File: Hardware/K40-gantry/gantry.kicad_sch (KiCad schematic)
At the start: 10 parts, among them U101 TCST1030, U102 TCST1030

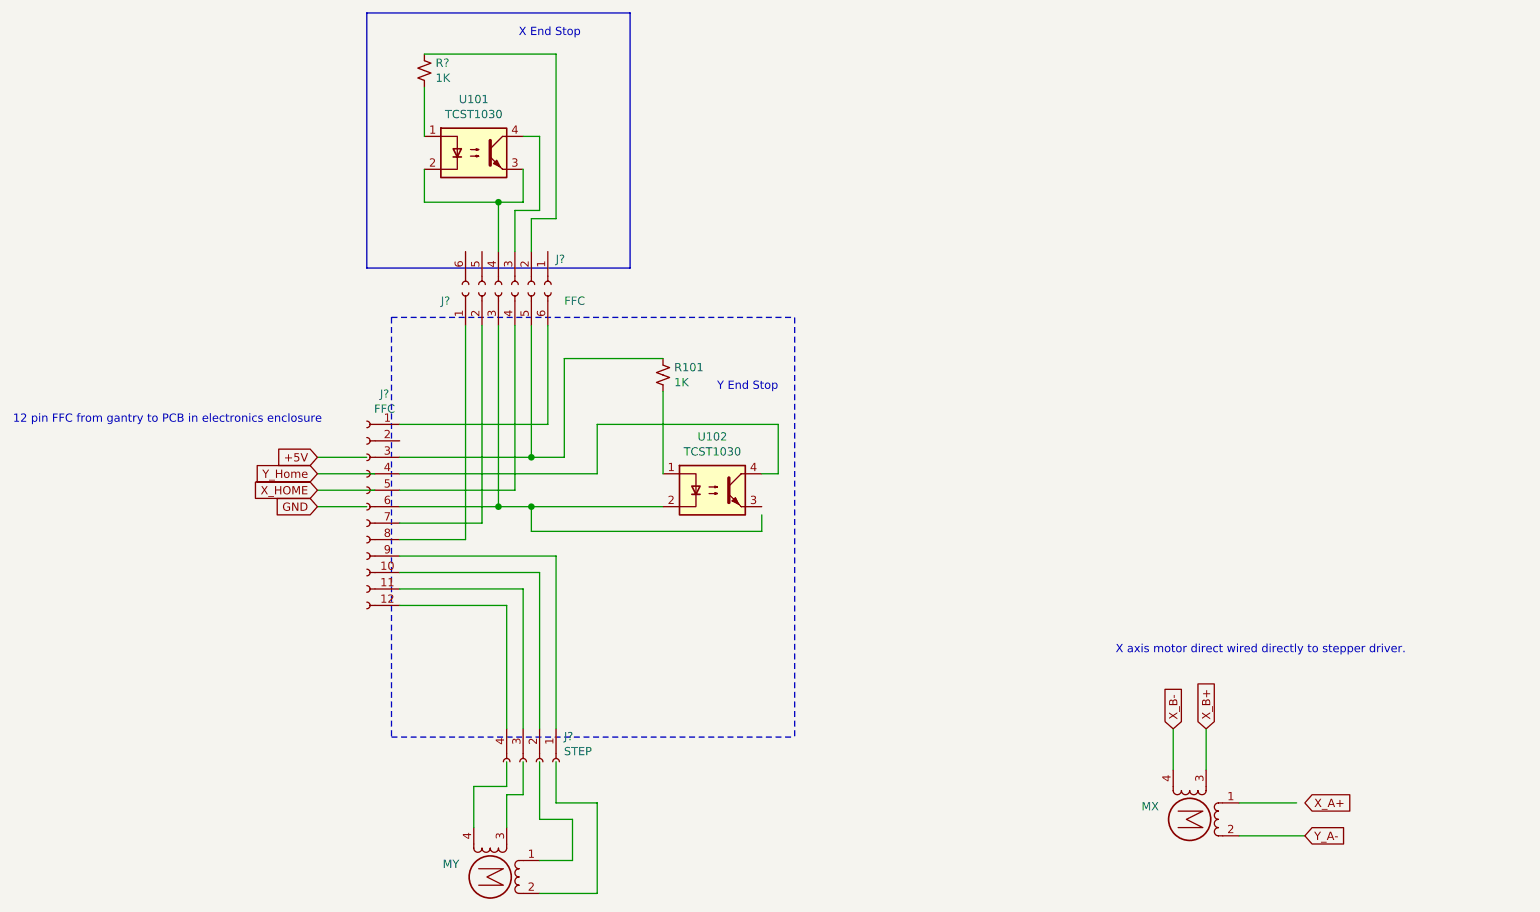
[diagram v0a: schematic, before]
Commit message: Added PDF of schematic
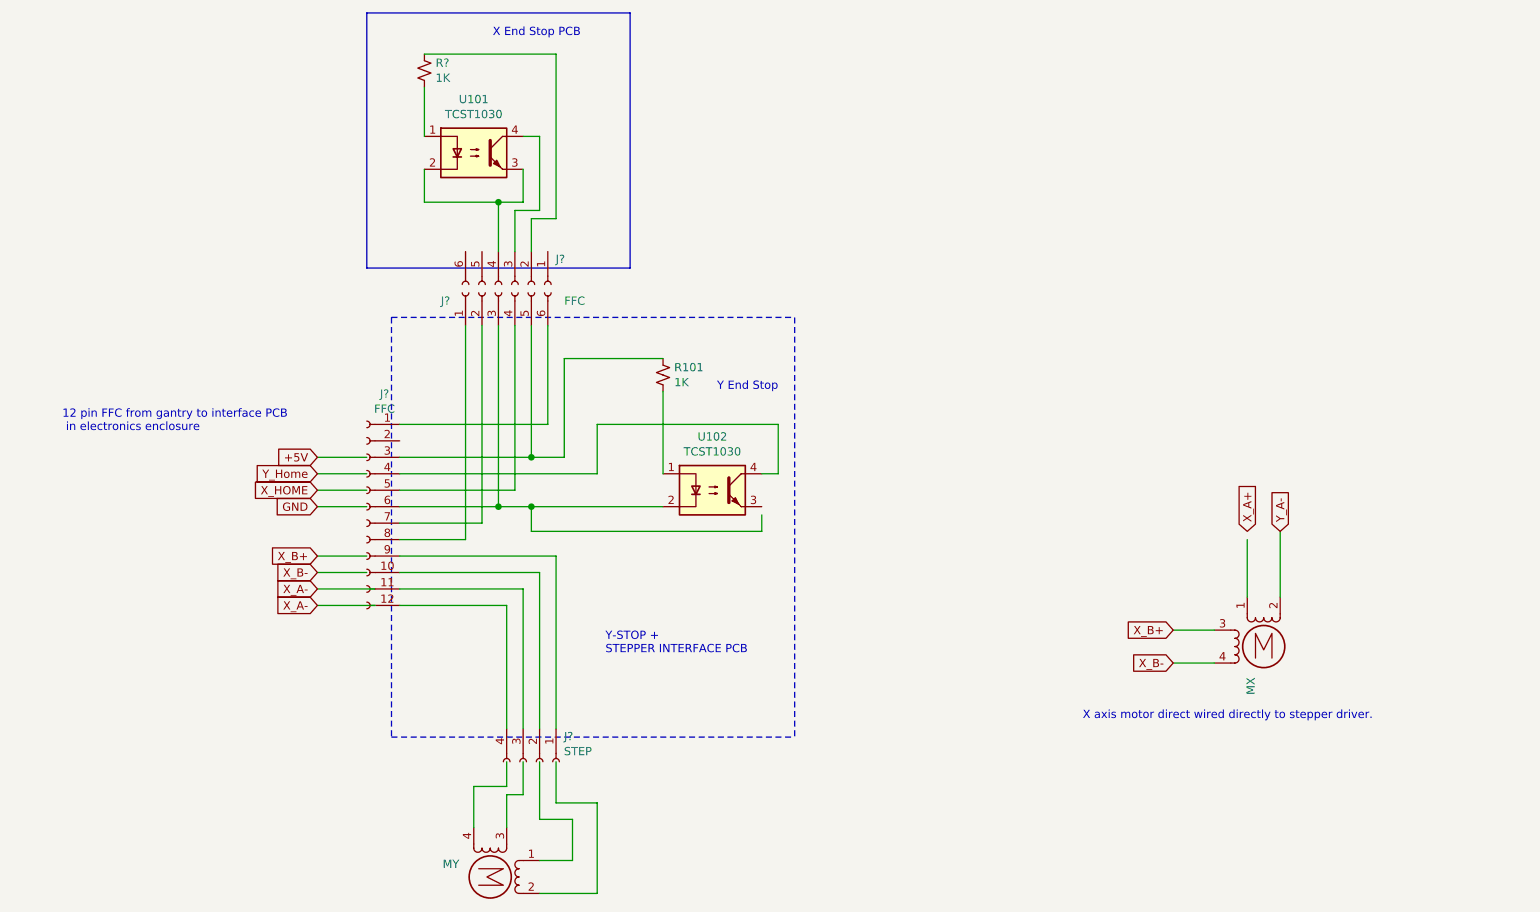
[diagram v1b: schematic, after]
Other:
- note added: "12 pin FFC from gantry to interface PCB in electronics enclosure"
- note added: "X End Stop PCB"
- note added: "Y-STOP + STEPPER INTERFACE PCB"
- note removed: "12 pin FFC from gantry to PCB in electronics enclosure"
- note removed: "X End Stop"
- company: Geoff Steer -> Hobart Makers
- moved on the sheet: MX
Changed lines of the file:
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@@
     (title "K40 Laser Gantry wiring")
     (date "2021-07-31")
-    (company "Geoff Steer")
+    (rev "1")
+    (company "Hobart Makers")
+    (comment 1 "Geoff Steer")
+    (comment 3 "Circuit diagram copied from https://donsthings.blogspot.com")
   )
   (junction (at 101.6 50.8) (diameter 1.016) (color 0 0 0 0))
@@
   (junction (at 106.68 90.17) (diameter 1.016) (color 0 0 0 0))
   (junction (at 106.68 97.79) (diameter 1.016) (color 0 0 0 0))
-  (wire (pts (xy 73.66 92.71) (xy 82.55 92.71))
-    (stroke (width 0) (type solid) (color 0 0 0 0))
-  )
-  (wire (pts (xy 73.66 95.25) (xy 82.55 95.25))
+  (wire (pts (xy 73.66 92.71) (xy 81.28 92.71))
+    (stroke (width 0) (type solid) (color 0 0 0 0))
+  )
+  (wire (pts (xy 73.66 95.25) (xy 81.28 95.25))
     (stroke (width 0) (type solid) (color 0 0 0 0))
   )
@@
     (stroke (width 0) (type solid) (color 0 0 0 0))
   )
+  (wire (pts (xy 73.66 105.41) (xy 81.28 105.41))
+    (stroke (width 0) (type solid) (color 0 0 0 0))
+  )
+  (wire (pts (xy 73.66 107.95) (xy 81.28 107.95))
+    (stroke (width 0) (type solid) (color 0 0 0 0))
+  )
+  (wire (pts (xy 73.66 110.49) (xy 82.55 110.49))
+    (stroke (width 0) (type solid) (color 0 0 0 0))
+  )
+  (wire (pts (xy 73.66 113.03) (xy 82.55 113.03))
+    (stroke (width 0) (type solid) (color 0 0 0 0))
+  )
   (wire (pts (xy 81.28 90.17) (xy 73.66 90.17))
     (stroke (width 0) (type solid) (color 0 0 0 0))
@@
     (stroke (width 0) (type solid) (color 0 0 0 0))
   )
-  (wire (pts (xy 205.74 138.43) (xy 205.74 132.08))
-    (stroke (width 0) (type solid) (color 0 0 0 0))
-  )
-  (wire (pts (xy 210.82 132.08) (xy 210.82 138.43))
-    (stroke (width 0) (type solid) (color 0 0 0 0))
-  )
-  (wire (pts (xy 224.79 143.51) (xy 215.9 143.51))
-    (stroke (width 0) (type solid) (color 0 0 0 0))
-  )
-  (wire (pts (xy 226.06 148.59) (xy 215.9 148.59))
+  (wire (pts (xy 205.74 116.84) (xy 212.09 116.84))
+    (stroke (width 0) (type solid) (color 0 0 0 0))
+  )
+  (wire (pts (xy 212.09 121.92) (xy 205.74 121.92))
+    (stroke (width 0) (type solid) (color 0 0 0 0))
+  )
+  (wire (pts (xy 217.17 102.87) (xy 217.17 111.76))
+    (stroke (width 0) (type solid) (color 0 0 0 0))
+  )
+  (wire (pts (xy 222.25 101.6) (xy 222.25 111.76))
     (stroke (width 0) (type solid) (color 0 0 0 0))
   )
@@
     (stroke (width 0) (type dash) (color 0 0 0 0))
   )
-  (text "12 pin FFC from gantry to PCB in electronics enclosure"
-    (at 26.67 85.09 0)
+  (text "12 pin FFC from gantry to interface PCB\n in electronics enclosure"
+    (at 34.29 86.36 0)
     (effects (font (size 1.27 1.27)) (justify left bottom))
   )
-  (text "X End Stop" (at 114.3 25.4 180)
+  (text "X End Stop PCB" (at 114.3 25.4 180)
     (effects (font (size 1.27 1.27)) (justify right bottom))
+  )
+  (text "Y-STOP + \nSTEPPER INTERFACE PCB" (at 118.11 120.65 0)
+    (effects (font (size 1.27 1.27)) (justify left bottom))
   )
   (text "Y End Stop" (at 144.78 80.01 180)
@@
   )
   (text "X axis motor direct wired directly to stepper driver."
-    (at 196.85 120.65 0)
+    (at 191.77 130.81 0)
     (effects (font (size 1.27 1.27)) (justify left bottom))
   )
@@
     )
   )
-  (global_label "X_B-" (shape input) (at 205.74 132.08 90) (fields_autoplaced)
+  (global_label "X_B+" (shape input) (at 73.66 105.41 180) (fields_autoplaced)
+    (effects (font (size 1.27 1.27)) (justify right))
+    (property "Intersheet References" "${INTERSHEET_REFS}" (id 0) (at -58.42 316.23 0)
+      (effects (font (size 1.27 1.27)) hide)
+    )
+  )
+  (global_label "X_B-" (shape input) (at 73.66 107.95 180) (fields_autoplaced)
+    (effects (font (size 1.27 1.27)) (justify right))
+    (property "Intersheet References" "${INTERSHEET_REFS}" (id 0) (at -58.42 313.69 0)
+      (effects (font (size 1.27 1.27)) hide)
+    )
+  )
+  (global_label "X_A-" (shape input) (at 73.66 110.49 180) (fields_autoplaced)
+    (effects (font (size 1.27 1.27)) (justify right))
+    (property "Intersheet References" "${INTERSHEET_REFS}" (id 0) (at 66.4088 110.4106 0)
+      (effects (font (size 1.27 1.27)) (justify right) hide)
+    )
+  )
+  (global_label "X_A-" (shape input) (at 73.66 113.03 180) (fields_autoplaced)
+    (effects (font (size 1.27 1.27)) (justify right))
+    (property "Intersheet References" "${INTERSHEET_REFS}" (id 0) (at 66.4088 112.9506 0)
+      (effects (font (size 1.27 1.27)) (justify right) hide)
+    )
+  )
+  (global_label "X_B+" (shape input) (at 205.74 116.84 180) (fields_autoplaced)
+    (effects (font (size 1.27 1.27)) (justify right))
+    (property "Intersheet References" "${INTERSHEET_REFS}" (id 0) (at 73.66 327.66 0)
+      (effects (font (size 1.27 1.27)) hide)
+    )
+  )
+  (global_label "X_B-" (shape input) (at 205.74 121.92 180) (fields_autoplaced)
+    (effects (font (size 1.27 1.27)) (justify right))
+    (property "Intersheet References" "${INTERSHEET_REFS}" (id 0) (at 73.66 327.66 0)
+      (effects (font (size 1.27 1.27)) hide)
+    )
+  )
+  (global_label "X_A+" (shape input) (at 217.17 101.6 90) (fields_autoplaced)
     (effects (font (size 1.27 1.27)) (justify left))
-    (property "Intersheet References" "${INTERSHEET_REFS}" (id 0) (at 0 0 0)
-      (effects (font (size 1.27 1.27)) hide)
-    )
-  )
-  (global_label "X_B+" (shape input) (at 210.82 132.08 90) (fields_autoplaced)
+    (property "Intersheet References" "${INTERSHEET_REFS}" (id 0) (at 73.66 327.66 0)
+      (effects (font (size 1.27 1.27)) hide)
+    )
+  )
+  (global_label "Y_A-" (shape input) (at 222.25 101.6 90) (fields_autoplaced)
     (effects (font (size 1.27 1.27)) (justify left))
-    (property "Intersheet References" "${INTERSHEET_REFS}" (id 0) (at 0 0 0)
-      (effects (font (size 1.27 1.27)) hide)
-    )
-  )
-  (global_label "X_A+" (shape input) (at 226.06 143.51 0) (fields_autoplaced)
-    (effects (font (size 1.27 1.27)) (justify left))
-    (property "Intersheet References" "${INTERSHEET_REFS}" (id 0) (at 0 0 0)
-      (effects (font (size 1.27 1.27)) hide)
-    )
-  )
-  (global_label "Y_A-" (shape input) (at 226.06 148.59 0) (fields_autoplaced)
-    (effects (font (size 1.27 1.27)) (justify left))
-    (property "Intersheet References" "${INTERSHEET_REFS}" (id 0) (at 0 0 0)
+    (property "Intersheet References" "${INTERSHEET_REFS}" (id 0) (at 73.66 327.66 0)
       (effects (font (size 1.27 1.27)) hide)
     )
@@
     (pin "4")
   )
-  (symbol (lib_id "Motor:Stepper_Motor_bipolar") (at 208.28 146.05 270) (unit 1)
-    (in_bom yes) (on_board yes)
-    (property "Reference" "MX" (id 0) (at 203.5302 144.0688 90)
+  (symbol (lib_id "Motor:Stepper_Motor_bipolar") (at 219.71 119.38 0) (unit 1)
+    (in_bom yes) (on_board yes)
+    (property "Reference" "MX" (id 0) (at 217.7288 124.1298 90)
       (effects (font (size 1.27 1.27)) (justify right))
     )
-    (property "Value" "Stepper_Motor_bipolar" (id 1) (at 203.5302 145.2118 90)
+    (property "Value" "Stepper_Motor_bipolar" (id 1) (at 218.8718 124.1298 90)
       (effects (font (size 1.27 1.27)) (justify right) hide)
     )
-    (property "Footprint" "" (id 2) (at 208.026 146.304 0)
-      (effects (font (size 1.27 1.27)) hide)
-    )
-    (property "Datasheet" "http://www.infineon.com/dgdl/Application-Note-TLE8110EE_driving_UniPolarStepperMotor_V1.1.pdf?fileId=db3a30431be39b97011be5d0aa0a00b0" (id 3) (at 208.026 146.304 0)
-      (effects (font (size 1.27 1.27)) hide)
-    )
+    (property "Footprint" "" (id 2) (at 219.964 119.634 0)
+      (effects (font (size 1.27 1.27)) hide)
+    )
+    (property "Datasheet" "http://www.infineon.com/dgdl/Application-Note-TLE8110EE_driving_UniPolarStepperMotor_V1.1.pdf?fileId=db3a30431be39b97011be5d0aa0a00b0" (id 3) (at 219.964 119.634 0)
+      (effects (font (size 1.27 1.27)) hide)
+    )
